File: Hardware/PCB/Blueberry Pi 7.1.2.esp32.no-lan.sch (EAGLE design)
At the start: 190 parts, among them IC2 E73_2G4M04S, J2 AUDIO_JACK_SMD, J3 USB-A-FEMALE, Q1 24Mhz, Q2 32kHz, Q3 IRLML2402, Q4 IRLML2402, U1 SN65LVDS84AQDGGRQ1, U2 W25Q32FV, U3 AP3031KTR-G1, U4 ESP-WROOM-32, X1 FH12-50S-0.5SH, X2 87758-1216

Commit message: added onboard li-ion/polimer battery charger, and step-up circuits for power from a li-battery.
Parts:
- removed IC1: (no value), v-reg-2:LM1117
- removed IC2: E73_2G4M04S, E73-2G4M04S:E73_2G4M04S
- removed JP3: (no value), pinhead-1:PINHD-1X6_2.00
- removed R24: 6k 1%, rcl:R-EU_R0603
- added C44: 10µF, rcl:C-EUC0805
- added D2, D6: (no value), diode:DIODE-DO214AC
- added D7: (no value), diode:DIODE-SOD323-W
- added J-BAT: 87758-0416, con-molex:87758-0416
- added L4: 2,2µH, rcl:L-EU
- added LED3, LED5: (no value), led:LEDCHIPLED_0805
- added R53, R58: 2k, rcl:R-EU_R0603
- added R54, R57, R59: 1k, rcl:R-EU_R0603
- added R55: 10k, rcl:R-EU_R0603
- added R56: 15k, rcl:R-EU_R0603
- added R60: 47k, rcl:R-EU_R0603
- added U$10: PT4101, PT4101:PT4101
- added U$14, U$6: MCP73831, mcp73831:MCP73831
- added U$15: XC6204, XC6204:XC6204XC6204
- C77: device resistor:C-EUC0805 -> resistor:C-EUC0603
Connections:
- removed net +3V3ANC: IC1.IN1
- removed net EPHY_RXN: U$1G$5.EPHY_RXN
- removed net EPHY_RXP: U$1G$5.EPHY_RXP
- removed net EPHY_TXN: U$1G$5.EPHY_TXN
- removed net EPHY_TXP: U$1G$5.EPHY_TXP
- removed net LINK_LED: U$1G$5.EPHY_LINK_LED
- removed net N$1: R24.1, U$1G$5.EPHY_RTX
- removed net SPD_LED: U$1G$5.EPHY_SPD_LED
- new net N$12: R55.1, R59.1, U$10.EN
- new net N$13: D7.A, L4.2, U$10.SW
- new net N$14: C44.1, U$10.IN
- new net N$19: R53.2, U$6.PROG
- new net N$35: LED3.C, R54.1
- new net N$38: R54.2, U$6.STAT
- new net N$4: D2.C, D6.C, L4.1, R59.2
- new net N$46: R58.2, U$14.PROG
- new net N$50: R57.2, U$14.STAT
- new net N$51: LED5.C, R57.1
- new net N$7: R56.1, R60.1, U$10.FB
- new net VIB1: U$7.V_BAT1, X2-11.S
- new net VIB2: U$7.V_BAT2, X2-12.S
- new net V_BAT1: D2.A, J-BAT-3.S, U$6.VBAT
- new net V_BAT2: D6.A, J-BAT-1.S, U$14.VBAT
- net +3V3A: now also U$15.VOUT; no longer IC1.OUT
- net +5V: now also D7.C, R60.2, U$10.OV, U$15.CE, U$15.VIN; no longer IC1.IN
- net GND: now also C44.2, J-BAT-2.S, J-BAT-4.S, R53.1, R55.2, R56.2, R58.1, U$10.GND, U$14.VSS, U$15.VSS, U$6.VSS; no longer IC1.GND, R24.2
- net V_PWR: now also LED3.A, LED5.A, U$14.VDD, U$6.VDD

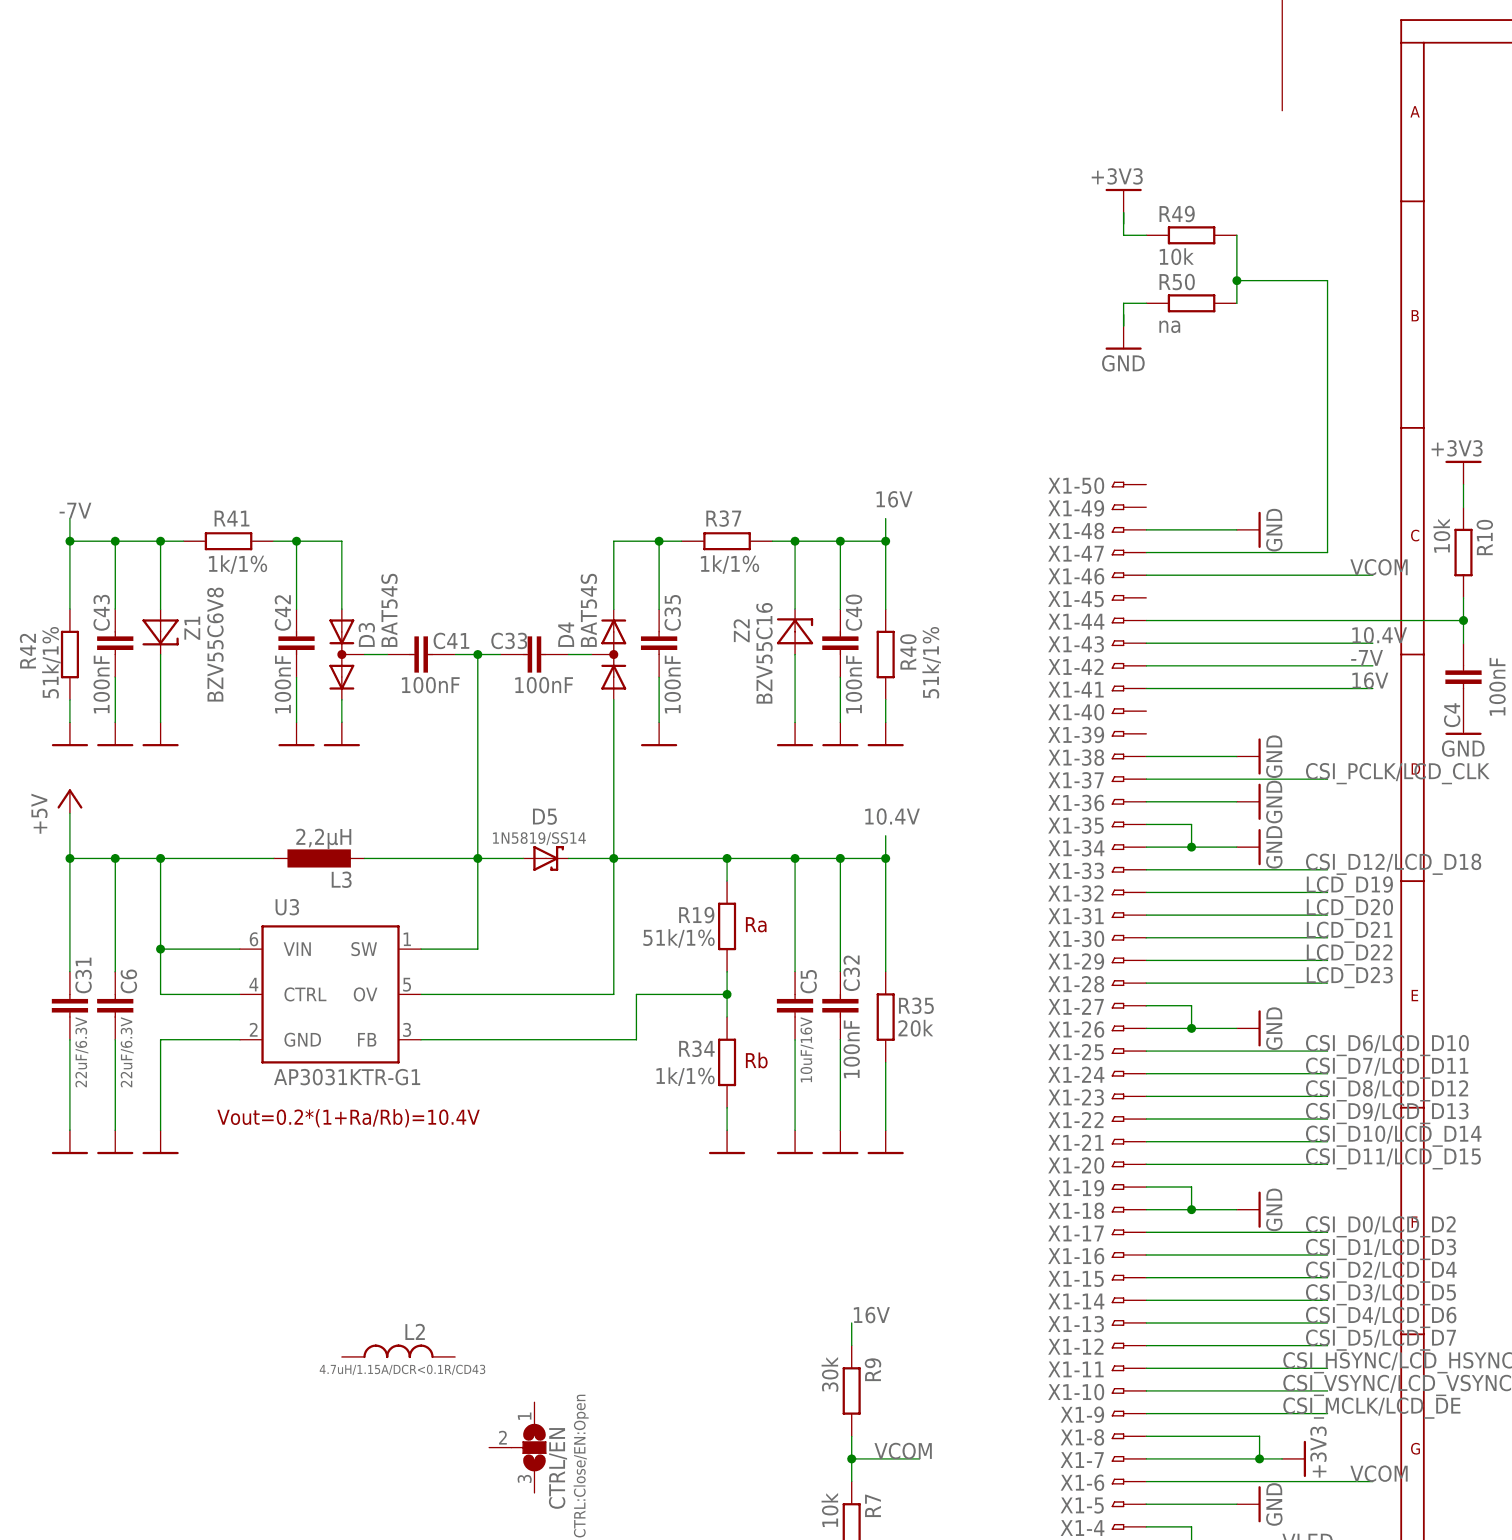
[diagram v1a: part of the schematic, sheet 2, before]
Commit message: added capacitive touch socket (not ready yet), other pwr-inductors (CD32), datasheets
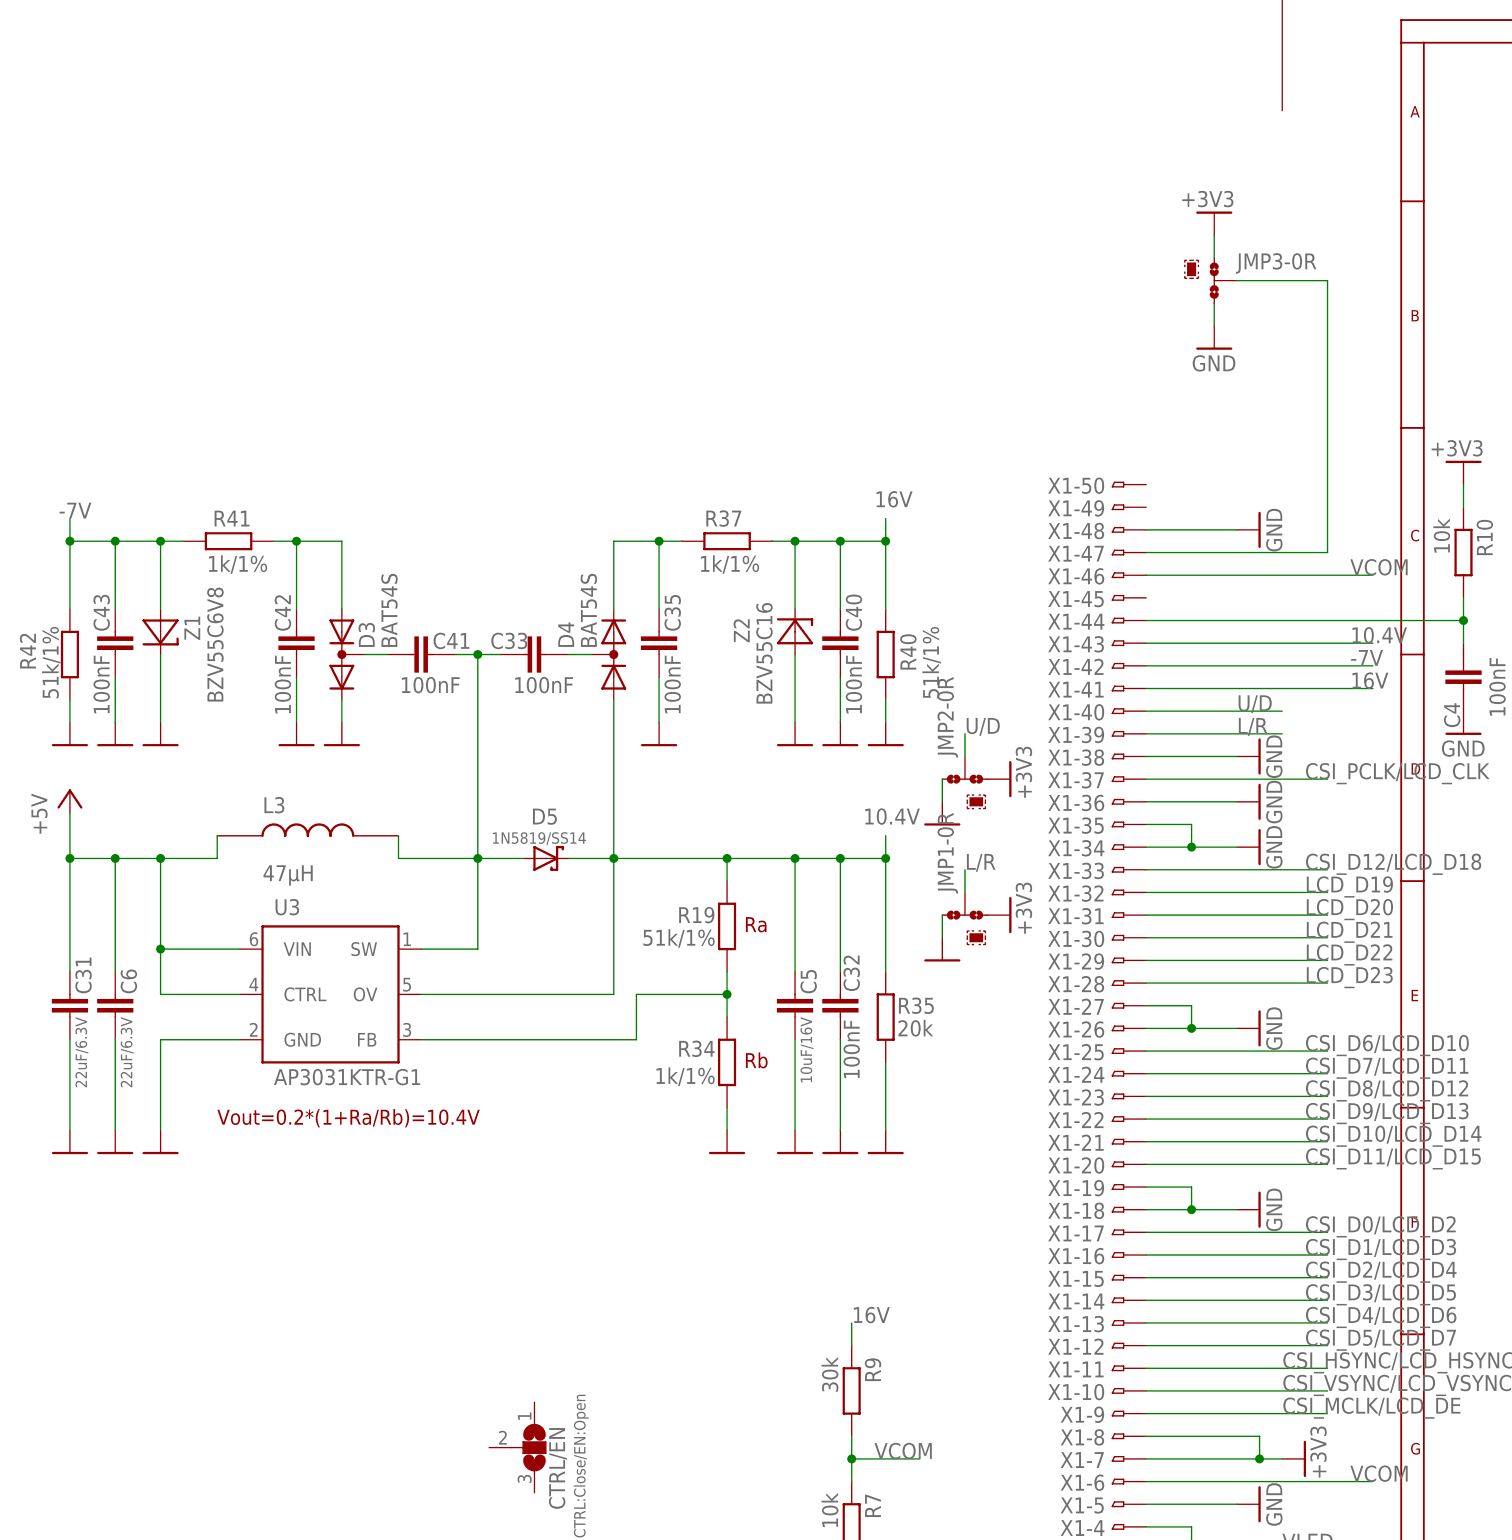
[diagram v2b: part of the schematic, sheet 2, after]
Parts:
- removed L2: 4.7uH/1.15A/DCR<0.1R/CD43, OLIMEX_DISCRET:L-CD42(43)
- removed R49: 10k, rcl:R-EU_R0603
- removed R50: na, rcl:R-EU_R0603
- added JMP1, JMP2, JMP3: 0R-JUMPC, jump-0r-smd:0R-JUMPC
- added U$21: FH12-06S-0.5S, con-hirose:FH12-06S-0.5S
- L1, L3: value 2,2µH -> 47µH; device rcl:L-EU -> induct-CD:INDUCTANCE_CD32
- L4: value 2,2µH -> 2.2uH; device rcl:L-EU -> induct-CD:INDUCTANCE_CD32
- L6, L7, L8: device rcl:L-EU -> induct-CD:INDUCTANCE_CD32
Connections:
- new net L/R: JMP1-0R.2, X1-39.1
- new net N$1: U$7.SCL
- new net N$18: U$7.SDA
- new net U/D: JMP2-0R.2, X1-40.1
- net +1V2: now also L6.P$1; no longer L6.1
- net +1V8: now also L7.P$1; no longer L7.1
- net +3V3: now also JMP1-0R.3, JMP2-0R.3, JMP3-0R.1, L8.P$1, U$21.2; no longer L8.1, R49.1
- net +5V: now also L1.P$1, L3.P$1; no longer L1.1, L3.1
- net GND: now also JMP1-0R.1, JMP2-0R.1, JMP3-0R.3, U$21.3; no longer R50.1
- net I2C1/SCL: now also U$21.6; no longer U$7.SCL
- net I2C1/SDA: now also U$21.5; no longer U$7.SDA
- net N$10: now also L1.P$2; no longer L1.2
- net N$123: now also L3.P$2; no longer L3.2
- net N$13: now also L4.P$2; no longer L4.2
- net N$16: now also L8.P$2; no longer L8.2
- net N$2: now also L6.P$2; no longer L6.2
- net N$24: now also JMP3-0R.2; no longer R49.2, R50.2
- net N$4: now also L4.P$1; no longer L4.1
- net N$5: now also L7.P$2; no longer L7.2
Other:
- moved on the sheet: C76, C79, C81

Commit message: interrupt pin for all touchscreens is PB3 shared with MIPI-CSI cam. basically added SPI-NOR-FLASH in the 16pins package (>= 32MB flashes)
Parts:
- added U$16: S25FL256S, Synapseware:S25FLSXXX
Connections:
- removed net N$1: U$7.SCL
- removed net N$18: U$7.SDA
- net +3V3: now also U$16./HOLD_IO3, U$16./WP_IO2, U$16.VCC
- net GND: now also U$16.VSS
- net I2C1/SCL: now also U$7.SCL
- net I2C1/SDA: now also U$7.SDA
- net PB3: now also U$21.4, U$7.!PENIRQ, U$8.PENIRQ
- net RESET: now also U$21.1
- net SPI1/CS: now also U$16./CS
- net SPI1/MISO: now also U$16.SO_IO1
- net SPI1/MOSI: now also U$16.SI_IO0
- net SPI1/SCK: now also U$16.SCK

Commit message: (not finished yet) checks and new choise with SIM800C gsm module
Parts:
- removed X2: 87758-1216, con-molex:87758-1216
- added J1: (no value), Wurth_Elektronik_Electromechanic_Input-Output_Connectors_rev16b:693023010811
- added J5: (no value), Wurth_Elektronik_Electromechanic_Input-Output_Connectors_rev16b:693043020611
- added U$17: SIM800C, SIM800C:SIM800C
- added U$18: HDR-1.27MM-62, headers-1.27:HDR-1.27MM-62
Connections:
- removed net N$4: D2.C, D6.C, L4.P$1, R59.2
- net +3V3: now also U$16./RST_RFU, U$18.7, U$18.8; no longer X2-7.S, X2-8.S
- net EA-IN1: now also U$18.9; no longer X2-9.S
- net EA-IN2: now also U$18.10; no longer X2-10.S
- net GND: now also U$18.5, U$18.6; no longer X2-5.S, X2-6.S
- net N$14: now also D2.C, D6.C, L4.P$1, R59.2
- net TPX1: now also U$18.1; no longer X2-1.S
- net TPX2: now also U$18.3; no longer X2-3.S
- net TPY1: now also U$18.2; no longer X2-2.S
- net TPY2: now also U$18.4; no longer X2-4.S
- net VIB1: now also U$18.11; no longer X2-11.S
- net VIB2: now also U$18.12; no longer X2-12.S
